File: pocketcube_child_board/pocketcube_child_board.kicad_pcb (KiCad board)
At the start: 2 copper layers, 50 x 50 mm, 5 parts, among them J1 M55-7102042R, U1 SI3477DV-T1-GE3

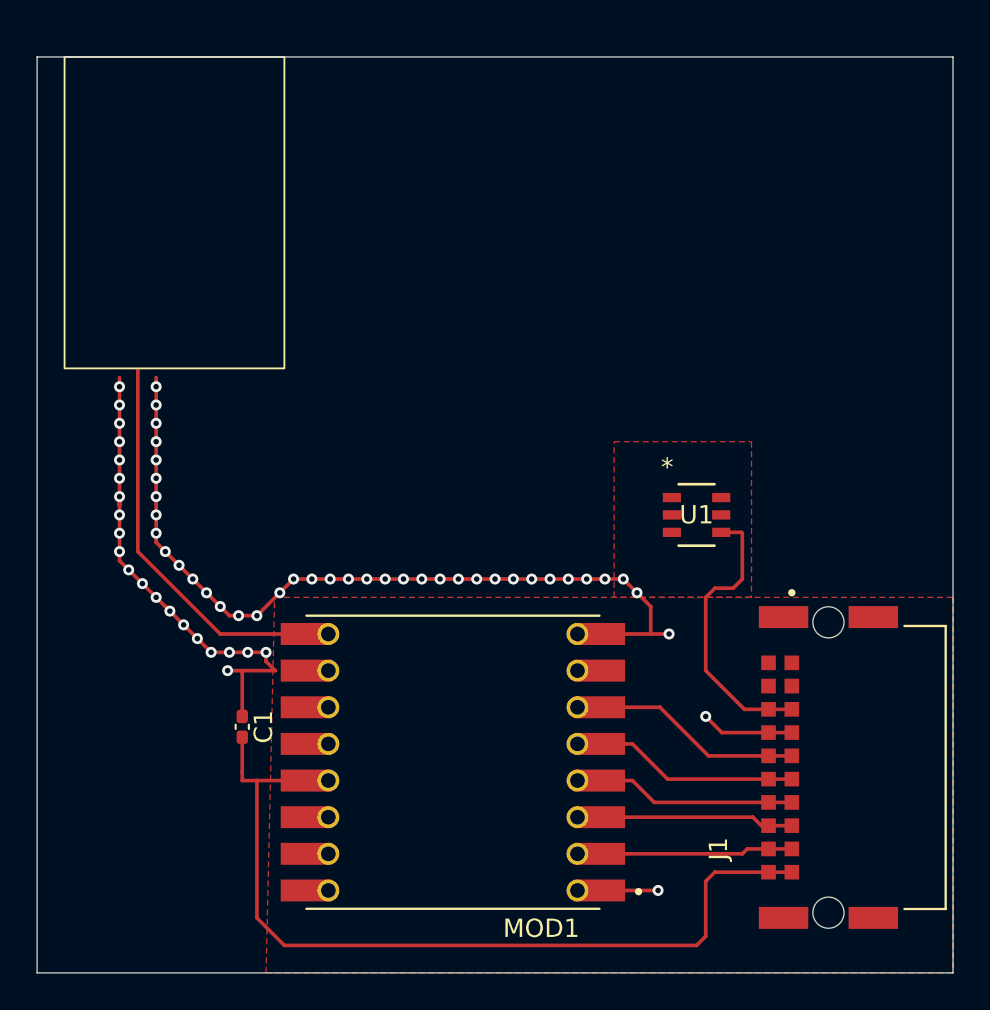
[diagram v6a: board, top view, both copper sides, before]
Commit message: implemented pmos
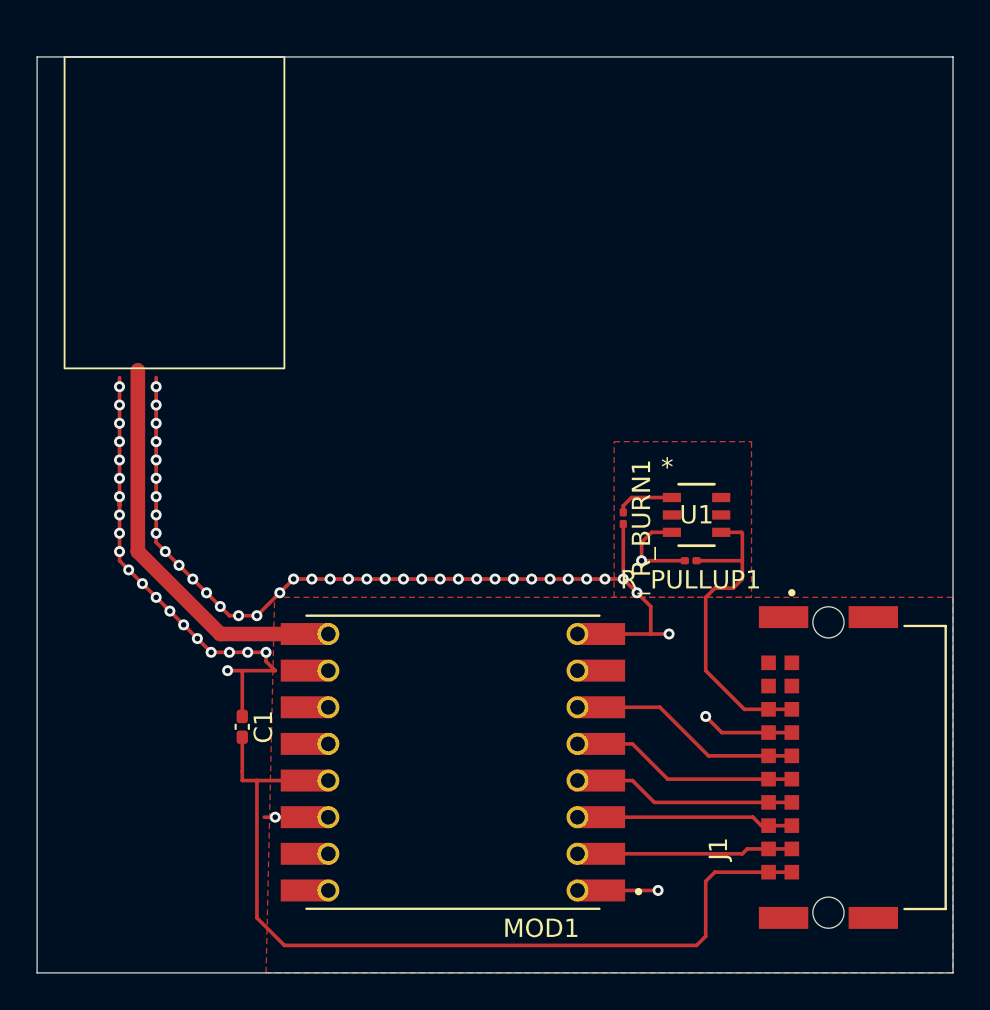
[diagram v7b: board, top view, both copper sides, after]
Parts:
- added R_BURN1: R, Resistor_SMD:R_0201_0603Metric, F.Cu at (120.0, 68.7)
- added R_PULLUP1: 10k, Resistor_SMD:R_0201_0603Metric, F.Cu at (123.7, 71.0)
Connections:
- MOD1 pad 14: unconnected-(MOD1-DIO0-Pad14) -> PMOS_GATE
- MOD1 pad 14_1: unconnected-(MOD1-DIO0__1-Pad14_1) -> PMOS_GATE
- U1 pad 1: unconnected-(U1-D-Pad1) -> Net-(R_BURN1-Pad1)
- U1 pad 3: unconnected-(U1-G-Pad3) -> DIO0
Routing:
- net DIO0: track 0.00 -> 5.24 mm, vias 0 -> 1
- net Net-(R_BURN1-Pad1): track 0.00 -> 3.20 mm
- net GND: track 80.1 -> 83.1 mm
- net 4.2V: track 15.7 -> 18.2 mm
- net PMOS_GATE: track 0.00 -> 2.30 mm, vias 0 -> 1

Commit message: PMOS Implementation and Ground Plane
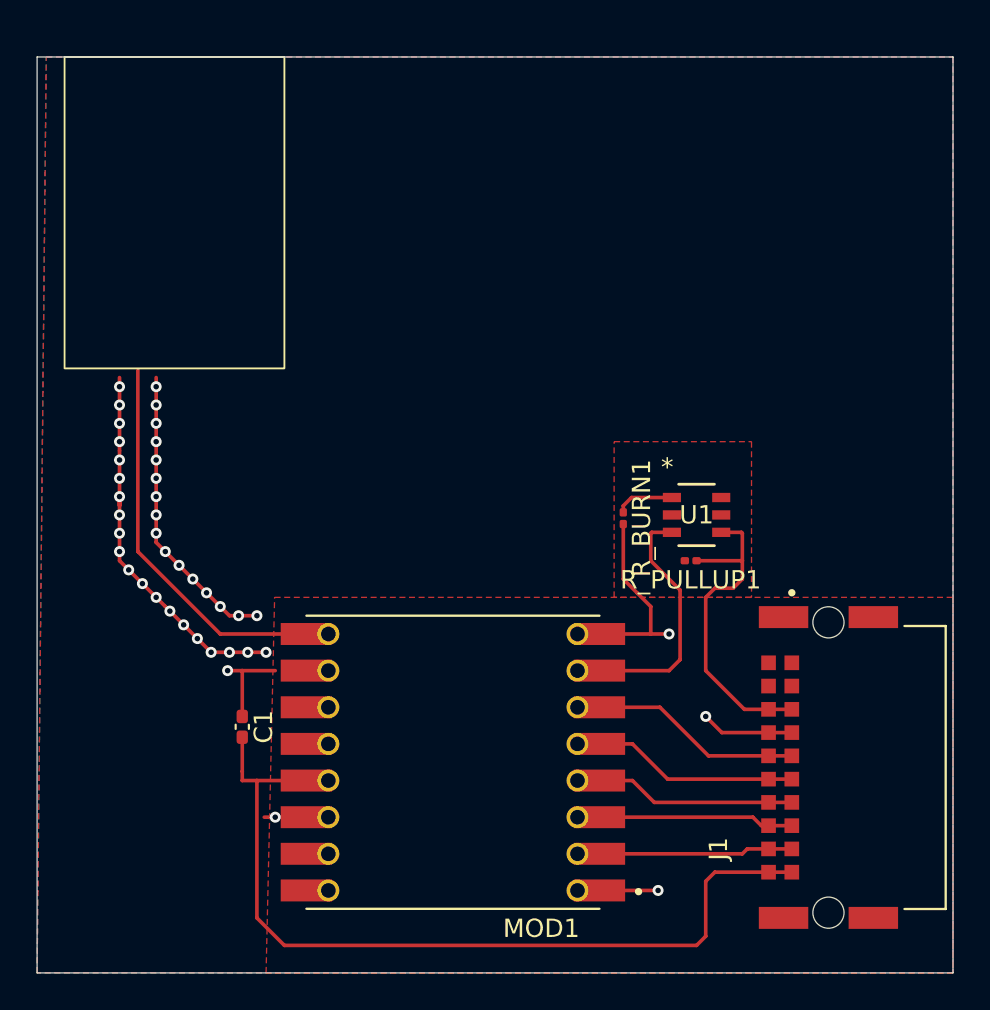
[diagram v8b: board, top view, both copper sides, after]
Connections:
- net Net-(AE1-A) renamed /ANTENNA_TRACE
- MOD1 pad 14: PMOS_GATE -> unconnected-(MOD1-DIO0-Pad14)
- MOD1 pad 14_1: PMOS_GATE -> unconnected-(MOD1-DIO0__1-Pad14_1)
- MOD1 pad 7: unconnected-(MOD1-DIO5-Pad7) -> PMOS_GATE
- MOD1 pad 7_1: unconnected-(MOD1-DIO5__1-Pad7_1) -> PMOS_GATE
- U1 pad 3: DIO0 -> PMOS_GATE
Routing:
- net GND: track 83.1 -> 61.0 mm, vias 61 -> 40
- net PMOS_GATE: track 2.30 -> 13.4 mm, vias 1 -> 0
- net DIO0: track 5.24 -> 0.00 mm, vias 1 -> 0
- net unconnected-(MOD1-DIO0-Pad14): track 0.00 -> 2.30 mm, vias 0 -> 1
- added copper zone on B.Cu, net GND
- added copper zone on F.Cu, net GND
